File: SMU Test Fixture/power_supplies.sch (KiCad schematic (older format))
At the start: 112 parts, among them Q1 Si2347DS, Q10 BC857, Q2 Si2347DS, Q3 BCP56, Q4 Si2347DS, Q5 Si2347DS, Q6 NJVMJB42CT4G, Q7 BCP56, Q8 BCP56, Q9 BCP56, T1 VPP12-4400, T2 VPP36-820, U10 MIC29510-5.0WT, U11 LT3045xMSE-1, U12 LT3094xMSE, U9 LM393

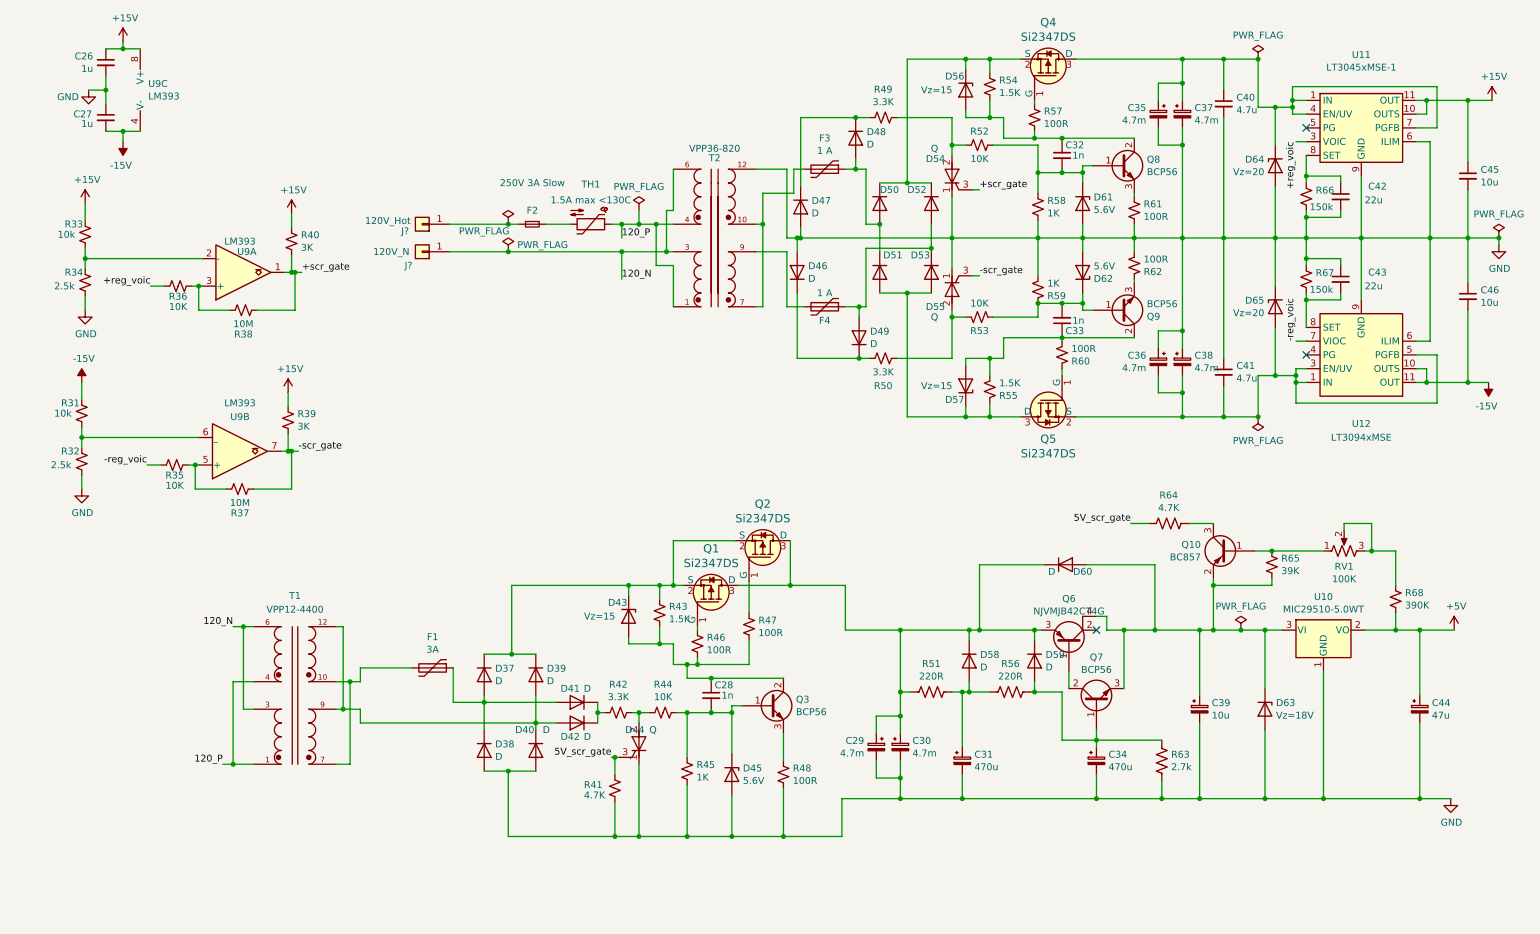
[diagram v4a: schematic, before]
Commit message: Comparator supply -> single-ended
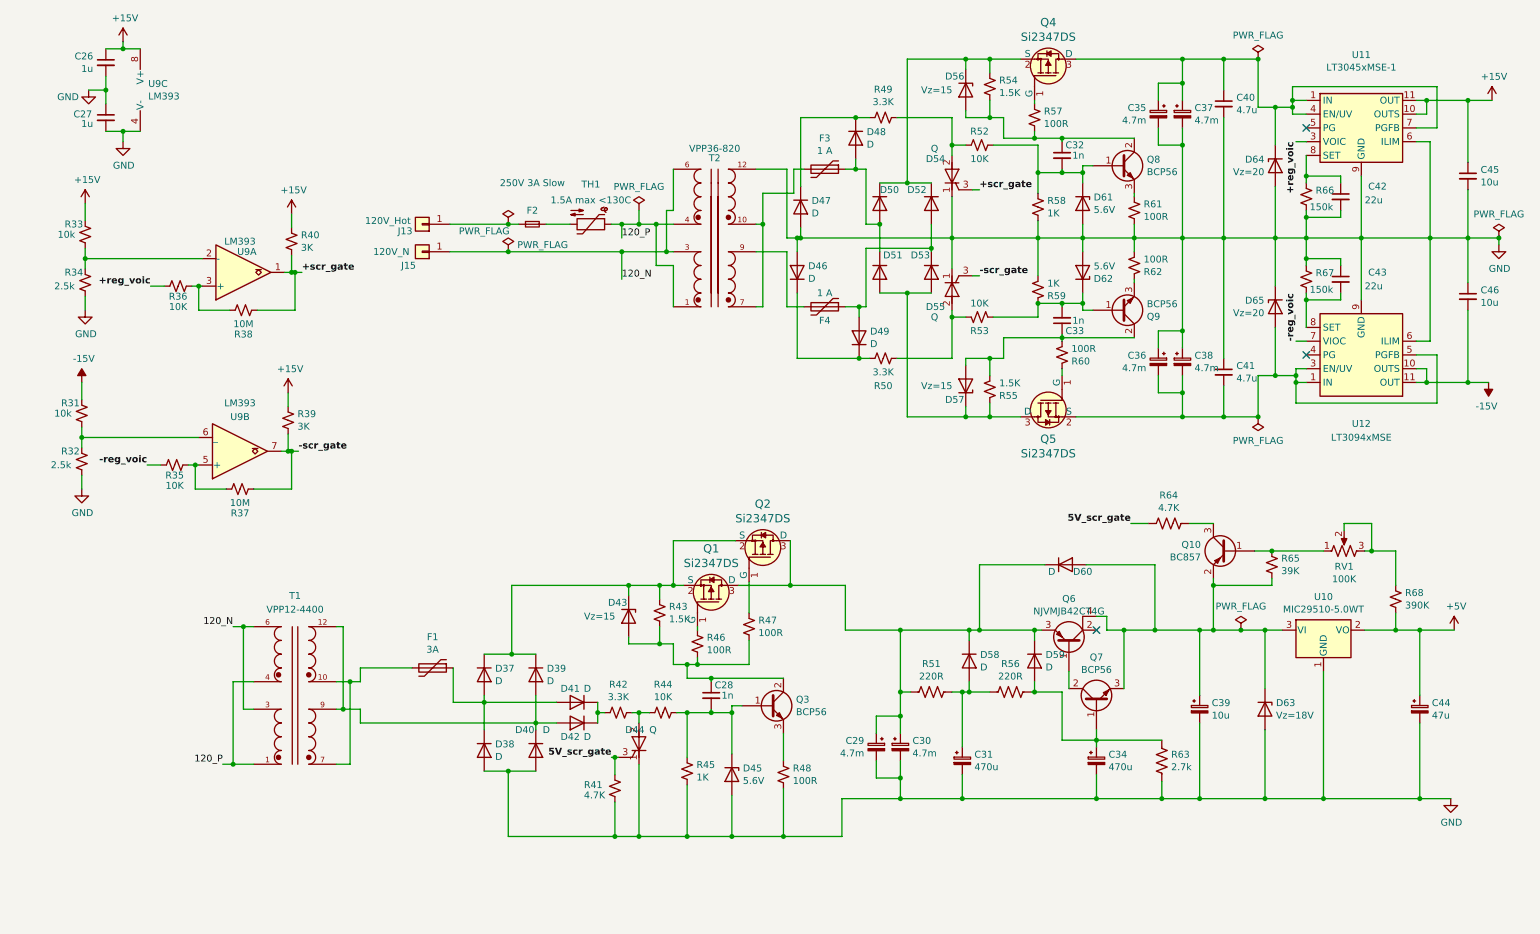
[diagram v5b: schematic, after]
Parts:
- gave numbers to parts that had none: 2
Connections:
- net -15V: no longer C27.2, U9.4 (V-)
- net GND: now also C27.2, U9.4 (V-)
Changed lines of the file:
@@
 Wire Wire Line
 	725  3650 725  3725
-Text Label 9550 1500 3    50   ~ 0
+Text Label 9550 1500 3    50   ~ 10
 +reg_voic
 Wire Wire Line
 	9550 1500 9625 1500
-Text Label 9550 2950 1    50   ~ 0
+Text Label 9550 2950 1    50   ~ 10
 -reg_voic
 Wire Wire Line
 	9550 2950 9625 2950
-Text Label 1200 3850 2    50   ~ 0
+Text Label 1200 3850 2    50   ~ 10
 -reg_voic
 $Comp
@@
 Wire Wire Line
 	1025 825  1150 825
-$Comp
-L power:-15V #PWR066
-U 1 1 6085D19D
-P 1025 1500
-F 0 "#PWR066" H 1025 1600 50  0001 C CNN
-F 1 "-15V" H 1040 1673 50  0000 C CNN
-F 2 "" H 1025 1500 50  0001 C CNN
-F 3 "" H 1025 1500 50  0001 C CNN
-	1    1025 1500
-	-1   0    0    1
-$EndComp
 Wire Wire Line
 	1025 1500 1025 1425
@@
 Wire Wire Line
 	7675 1725 7675 1875
-Text Label 2300 3750 0    50   ~ 0
+Text Label 2300 3750 0    50   ~ 10
 -scr_gate
 Wire Wire Line
@@
 Wire Wire Line
 	1200 3850 1300 3850
-Text Label 7250 1850 0    50   ~ 0
+Text Label 7250 1850 0    50   ~ 10
 +scr_gate
 $Comp
@@
 Wire Wire Line
 	750  2350 750  2425
-Text Label 1225 2550 2    50   ~ 0
+Text Label 1225 2550 2    50   ~ 10
 +reg_voic
 $Comp
@@
 	1    0    0    -1
 $EndComp
-Text Label 2325 2450 0    50   ~ 0
+Text Label 2325 2450 0    50   ~ 10
 +scr_gate
 Wire Wire Line
@@
 Wire Wire Line
 	7250 2475 7200 2475
-Text Label 7250 2475 0    50   ~ 0
+Text Label 7250 2475 0    50   ~ 10
 -scr_gate
 $Comp
@@
 Wire Wire Line
 	4775 6025 4775 6550
-Text Label 4575 5975 2    50   ~ 0
+Text Label 4575 5975 2    50   ~ 10
 5V_scr_gate
 Wire Wire Line
@@
 Wire Wire Line
 	8950 4275 8775 4275
-Text Label 8350 4275 2    50   ~ 0
+Text Label 8350 4275 2    50   ~ 10
 5V_scr_gate
 Wire Wire Line
@@
 $EndComp
 $Comp
-L Connector_Generic:Conn_01x01 J?
+L Connector_Generic:Conn_01x01 J13
 U 1 1 601511D3
 P 3200 2100
-F 0 "J?" H 3325 2150 50  0000 C CNN
+F 0 "J13" H 3325 2150 50  0000 C CNN
 F 1 "120V_Hot" H 3450 2075 50  0000 C CNN
 F 2 "Connector_Wire:SolderWire-0.75sqmm_1x01_D1.25mm_OD2.3mm" H 3200 2100 50  0001 C CNN
@@
 $EndComp
 $Comp
-L Connector_Generic:Conn_01x01 J?
+L Connector_Generic:Conn_01x01 J15
 U 1 1 60151E3B
 P 3200 2300
-F 0 "J?" H 3300 2400 50  0000 C CNN
+F 0 "J15" H 3300 2400 50  0000 C CNN
 F 1 "120V_N" H 3425 2300 50  0000 C CNN
 F 2 "Connector_Wire:SolderWire-0.75sqmm_1x01_D1.25mm_OD2.3mm" H 3200 2300 50  0001 C CNN
@@
 	-1   0    0    1
 $EndComp
+$Comp
+L power:GND #PWR?
+U 1 1 603456AB
+P 1025 1500
+F 0 "#PWR?" H 1025 1250 50  0001 C CNN
+F 1 "GND" H 1030 1327 50  0000 C CNN
+F 2 "" H 1025 1500 50  0001 C CNN
+F 3 "" H 1025 1500 50  0001 C CNN
+	1    1025 1500
+	1    0    0    -1
+$EndComp
 $EndSCHEMATC

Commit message: Switch to 28V txfrmr, nix preregs, nix 5V for AD2, switch to 12V relay power.
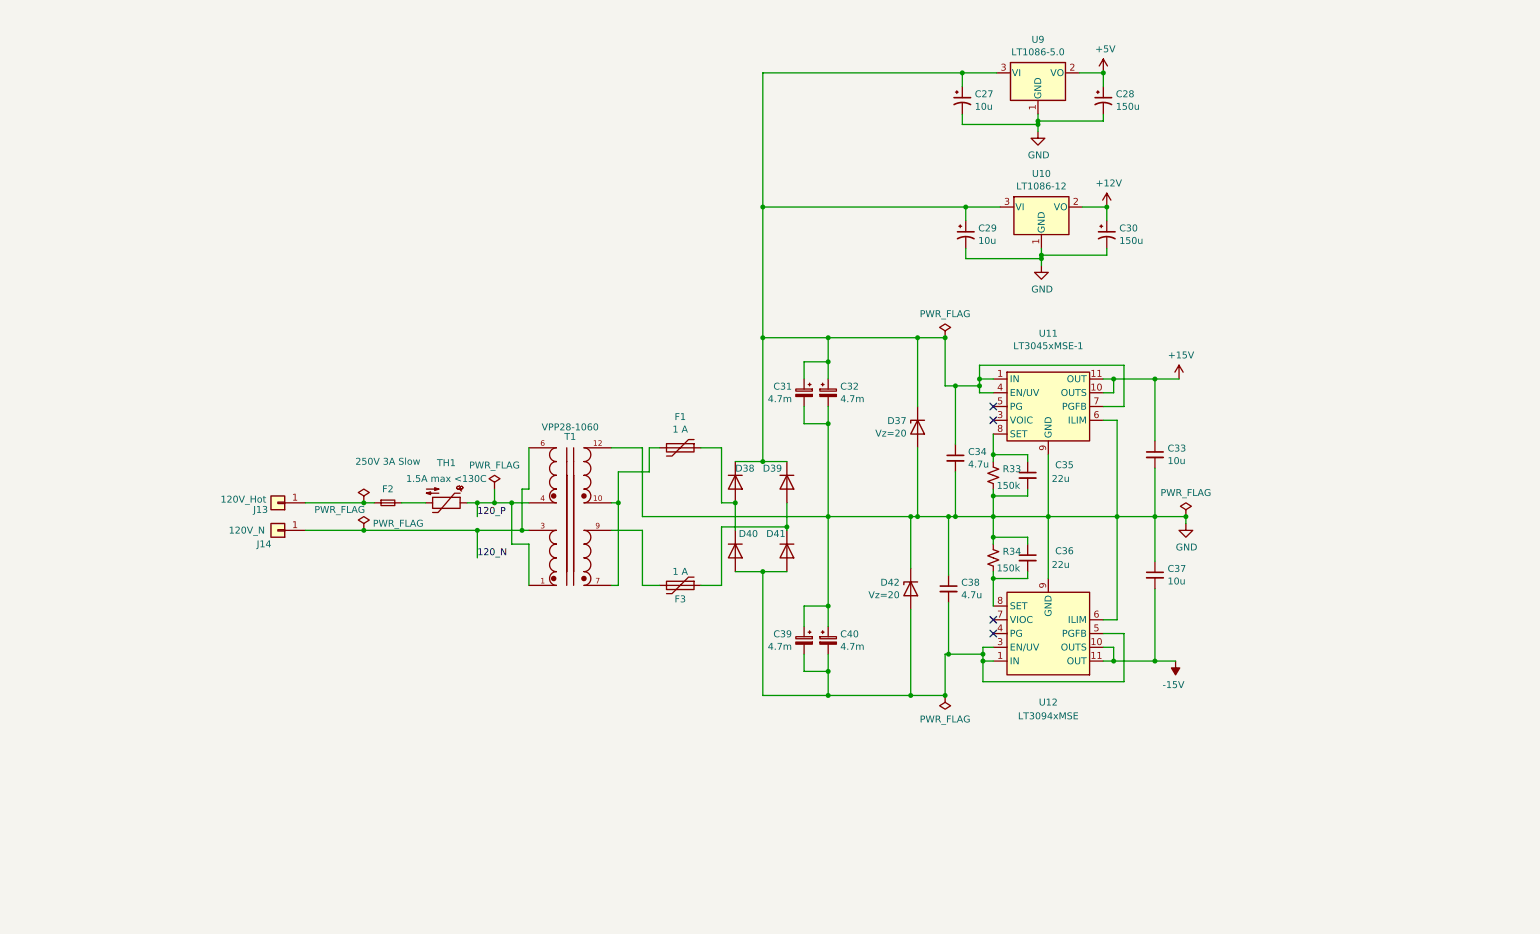
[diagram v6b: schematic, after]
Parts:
- removed C26, C27: 1u, Capacitor_SMD:C_0805_2012Metric_Pad1.18x1.45mm_HandSolder, symbol Device:C_Small
- removed C28, C32, C33: 1n, Capacitor_SMD:C_0805_2012Metric_Pad1.18x1.45mm_HandSolder, symbol Device:C_Small
- removed C29, C30: 4.7m, Capacitor_THT:CP_Radial_D22.0mm_P10.00mm_SnapIn, symbol Device:CP_Small
- removed C31, C34: 470u, Capacitor_THT:CP_Radial_D12.5mm_P5.00mm, symbol Device:CP_Small
- removed C39: 10u, Capacitor_SMD:C_Elec_5x5.8, symbol Device:CP_Small
- removed C40: 4.7u, Capacitor_SMD:C_0805_2012Metric_Pad1.18x1.45mm_HandSolder, symbol Device:C_Small
- removed C44: 47u, Capacitor_SMD:CP_Elec_8x10, symbol Device:CP_Small
- removed D37, D38, D39, D40: D, Package_TO_SOT_SMD:TO-263-3_TabPin2, symbol Device:D
- removed D41, D42, D46, D47, D48, D49, D58, D59, D60: D, Diode_SMD:D_SOD-123, symbol Device:D
- removed D43, D56, D57: Vz=15, Package_TO_SOT_SMD:SOT-323_SC-70_Handsoldering, symbol Device:D_Zener
- removed D44, D54, D55: Q, Package_TO_SOT_SMD:SOT-323_SC-70_Handsoldering, symbol Device:Q_SCR_KAG
- removed D45: 5.6V, Diode_SMD:D_SOD-323_HandSoldering, symbol Device:D_Zener
- removed D61, D62: 5.6V, Capacitor_SMD:C_0805_2012Metric_Pad1.18x1.45mm_HandSolder, symbol Device:D_Zener
- removed D63: Vz=18V, Diode_SMD:D_SOD-523, symbol Device:D_Zener
- removed F1: 3A, Fuse:Fuse_1812_4532Metric_Pad1.30x3.40mm_HandSolder, symbol Device:Polyfuse
- removed Q1, Q2, Q4, Q5: Si2347DS, digikey-footprints:SOT-23-3, symbol dk_Transistors-FETs-MOSFETs-Single:DMG2305UX-13
- removed Q10: BC857, Package_TO_SOT_SMD:SOT-23, symbol Transistor_BJT:BC857
- removed Q3, Q7, Q8, Q9: BCP56, Package_TO_SOT_SMD:SOT-223-3_TabPin2, symbol Transistor_BJT:BCP56
- removed Q6: NJVMJB42CT4G, Package_TO_SOT_SMD:TO-263-3_TabPin4, symbol Device:Q_PNP_BCEC
- removed R31, R33: 10k, Resistor_SMD:R_0805_2012Metric_Pad1.20x1.40mm_HandSolder, symbol Device:R_Small_US
- removed R32, R34: 2.5k, Resistor_SMD:R_0805_2012Metric_Pad1.20x1.40mm_HandSolder, symbol Device:R_Small_US
- removed R35, R36, R44, R52, R53: 10K, Resistor_SMD:R_0805_2012Metric_Pad1.20x1.40mm_HandSolder, symbol Device:R_Small_US
- removed R37, R38: 10M, Resistor_SMD:R_0805_2012Metric_Pad1.20x1.40mm_HandSolder, symbol Device:R_Small_US
- removed R39, R40: 3K, Resistor_SMD:R_0805_2012Metric_Pad1.20x1.40mm_HandSolder, symbol Device:R_Small_US
- removed R41: 4.7K, Resistor_SMD:R_0805_2012Metric_Pad1.20x1.40mm_HandSolder, symbol Device:R_Small_US
- removed R42, R49, R50: 3.3K, Resistor_SMD:R_0805_2012Metric_Pad1.20x1.40mm_HandSolder, symbol Device:R_Small_US
- removed R43, R54, R55: 1.5K, Resistor_SMD:R_0805_2012Metric_Pad1.20x1.40mm_HandSolder, symbol Device:R_Small_US
- removed R45, R58, R59: 1K, Resistor_SMD:R_0805_2012Metric_Pad1.20x1.40mm_HandSolder, symbol Device:R_Small_US
- removed R46, R47, R48, R57, R60, R61, R62: 100R, Resistor_SMD:R_0805_2012Metric_Pad1.20x1.40mm_HandSolder, symbol Device:R_Small_US
- removed R51, R56: 220R, Resistor_SMD:R_0805_2012Metric_Pad1.20x1.40mm_HandSolder, symbol Device:R_US
- removed R63: 2.7k, Resistor_SMD:R_0805_2012Metric_Pad1.20x1.40mm_HandSolder, symbol Device:R_US
- removed R64: 4.7K, Resistor_SMD:R_0805_2012Metric_Pad1.20x1.40mm_HandSolder, symbol Device:R_US
- removed R65: 39K, Resistor_SMD:R_0805_2012Metric_Pad1.20x1.40mm_HandSolder, symbol Device:R_Small_US
- removed R68: 390K, Resistor_SMD:R_0805_2012Metric_Pad1.20x1.40mm_HandSolder, symbol Device:R_Small_US
- removed RV1: 100K, Potentiometer_SMD:Potentiometer_Bourns_TC33X_Vertical, symbol Device:R_POT_US
- removed T1: VPP12-4400, eaton:XFMR_VPP12-4400, symbol multiplexer:VPP12-4400
- removed U10: MIC29510-5.0WT, Package_TO_SOT_THT:TO-220-3_Vertical, symbol Regulator_Linear:LT1083-5.0
- removed U9: LM393, Package_SO:TSSOP-8_4.4x3mm_P0.65mm, symbol Comparator:LM393
- added C27, C29: 10u, symbol Device:CP1_Small
- added C28, C30: 150u, symbol Device:CP1_Small
- added C34: 4.7u, Capacitor_SMD:C_0805_2012Metric_Pad1.18x1.45mm_HandSolder, symbol Device:C_Small
- added U10: LT1086-12, symbol Regulator_Linear:LT1086-12
- added U9: LT1086-5.0, symbol Regulator_Linear:LT1086-5.0
- T1: renamed from T2; value VPP36-820 -> VPP28-1060; footprint eaton:XFMR_VPP36-820 -> eaton:XFMR_VPP28-1060; PN VPP36-820 -> VPP28-1060
- renumbered C35 to C31, C37 to C32, C45 to C33, C42 to C35, C43 to C36, C46 to C37, C41 to C38, C36 to C39, C38 to C40, D64 to D37, D50 to D38, D52 to D39, D51 to D40, D53 to D41, D65 to D42, F3 to F1, F4 to F3, J15 to J14, R66 to R33, R67 to R34
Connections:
- net +5V: now also C28.1, U9.2 (VO)
- net GND: now also C27.2, C28.2, C29.2, C30.2, C34.2, U10.1 (GND), U9.1 (GND)
- net at C38.2, C39.2, C40.2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: now also D40.2 (A), D41.2 (A)
- net at C31.1, C32.1, D37.1 (K)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: now also D38.1 (K), D39.1 (K), C27.1, C29.1, C34.1, U10.3 (VI), U9.3 (VI)
- net +reg_voic: no longer names the net of U11.3 (VOIC)
- net -reg_voic: no longer names the net of U12.7 (VIOC)
- new net +12V: C30.1, U10.2 (VO)
- no-connect marks 3 -> 4
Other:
- moved on the sheet: C31, C32, C33, C35, C36, C37, C38, C39, C40, D37, D38, D39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

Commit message: Reannotate, power supply schematic improvements, begin power supply layout.
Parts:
- removed C29: 10u, symbol Device:CP1_Small
- removed C30: 150u, symbol Device:CP1_Small
- removed D37, D42: Vz=20, Diode_SMD:D_SOD-523, symbol Device:D_Zener
- removed F2: 250V 3A Slow, symbol Device:Fuse_Small
- removed J13: 120V_Hot, Connector_Wire:SolderWire-0.75sqmm_1x01_D1.25mm_OD2.3mm, symbol Connector_Generic:Conn_01x01
- removed J14: 120V_N, Connector_Wire:SolderWire-0.75sqmm_1x01_D1.25mm_OD2.3mm, symbol Connector_Generic:Conn_01x01
- added C37: 10u, Capacitor_SMD:CP_Elec_6.3x5.8, symbol Device:CP1_Small
- added C38: 150u, Capacitor_SMD:CP_Elec_10x10, symbol Device:CP1_Small
- added D39: 20V Clamp, Package_TO_SOT_SMD:SOT-323_SC-70_Handsoldering, symbol Device:D_TVS_x2_AAC
- added D42, D43, D44, D45: LED, LED_THT:LED_D3.0mm_Horizontal_O6.35mm_Z2.0mm, symbol Device:LED
- added J13: Hot_Spade, MAGI_Footprints:p250_spade, symbol Connector:Conn_01x01_Male
- added J14: Power Outputs, Connector_PinHeader_2.54mm:PinHeader_1x05_P2.54mm_Horizontal, symbol Connector:Conn_01x05_Male
- added J15: Neutral_Spade, MAGI_Footprints:p250_spade, symbol Connector:Conn_01x01_Male
- added R33, R34: 750R, Resistor_SMD:R_0805_2012Metric_Pad1.20x1.40mm_HandSolder, symbol Device:R_Small_US
- added R35: 270R, Resistor_SMD:R_0805_2012Metric_Pad1.20x1.40mm_HandSolder, symbol Device:R_Small_US
- added R36: 620R, Resistor_SMD:R_0805_2012Metric_Pad1.20x1.40mm_HandSolder, symbol Device:R_Small_US
- added THJ1, THJ2: Thermal Jumper, Capacitor_SMD:C_0805_2012Metric_Pad1.18x1.45mm_HandSolder, symbol Device:MEMRISTOR
- C27: renamed from C31; footprint Capacitor_THT:CP_Radial_D22.0mm_P10.00mm_SnapIn -> MAGI_Footprints:d=22_L=50_Radial_Horiz_P=10
- C28: renamed from C32; footprint Capacitor_THT:CP_Radial_D22.0mm_P10.00mm_SnapIn -> MAGI_Footprints:d=22_L=50_Radial_Horiz_P=10
- C29: renamed from C39; footprint Capacitor_THT:CP_Radial_D22.0mm_P10.00mm_SnapIn -> MAGI_Footprints:d=22_L=50_Radial_Horiz_P=10
- C30: renamed from C40; footprint Capacitor_THT:CP_Radial_D22.0mm_P10.00mm_SnapIn -> MAGI_Footprints:d=22_L=50_Radial_Horiz_P=10
- C31: renamed from C27; footprint (none) -> Capacitor_SMD:CP_Elec_6.3x5.8; PN (none) -> UUD1H100MCL1GS
- C32: renamed from C28; footprint (none) -> Capacitor_SMD:CP_Elec_10x10; PN (none) -> UUD1H151MNL1GS
- T1: footprint eaton:XFMR_VPP28-1060 -> MAGI_Footprints:XFMR_VPP28-1060; symbol multiplexer:VPP36-820 -> MAGI_Symbols:VPP28-1060
- TH1: value 1.5A max <130C -> 3.5A max <130C; footprint eaton:NTC d=11.5 p=5mm w=6mm -> MAGI_Footprints:NTC d=11.5 p=5mm w=6mm; PN B57236S0121M051 -> B57236S0100M000
- U10: renamed from U11; symbol multiplexer:LT3045xMSE-1 -> MAGI_Symbols:LT3045xMSE-1
- U11: renamed from U10; footprint (none) -> Package_TO_SOT_THT:TO-220-3_Vertical
- U9: footprint (none) -> Package_TO_SOT_THT:TO-220-3_Vertical
- renumbered C37 to C39, C38 to C40, D38 to D37, D39 to D38, F3 to F2, R33 to R37, R34 to R38
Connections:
- net labels added: unreg_neg_18VDC, unreg_pos_18VDC
- net labels removed: 120_N, 120_P
- wire segments 172 -> 197
- no-connect marks 4 -> 8
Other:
- note added: "+ 12 V for relays"
- note added: "+ 15V for analog section"
- note added: "+ 5V for aux / pH meter"
- note added: "- 15V for analog section"
- note added: "LT3045 bottom pad is input.\nUse thermal jumpers to\nconduct into ground."
- note added: "Mains input and rectification"
- note added: "Output Connector"
- note added: "Output Indicators"
- note added: "To BVB01/Z0000/10\nSwitchable, fused, power entry module\n3.5A Slow Blow"
- moved on the sheet: C27, C28, C29, C30, C31, C32, C33, C34, C35, C36, C39, C40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

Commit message: Change power entry module to fit enclosure.
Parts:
- C27, C28, C30: value 4.7m -> 510u; footprint MAGI_Footprints:d=22_L=50_Radial_Horiz_P=10 -> Capacitor_SMD:CP_Elec_18x22; PN UVY1J472MRD -> UCM2A511MNJ1MS
- C29: value 4.7m -> 510u; footprint MAGI_Footprints:d=22_L=50_Radial_Horiz_P=10 -> Capacitor_SMD:CP_Elec_18x22
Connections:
- wire segments 197 -> 201
- no-connect marks 8 -> 4
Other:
- note added: "To BZH01/Z0000/01\nSwitchable, fused, power entry module\n3.5A Slow Blow"
- note removed: "To BVB01/Z0000/10\nSwitchable, fused, power entry module\n3.5A Slow Blow"
